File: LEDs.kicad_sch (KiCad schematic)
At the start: 14 parts

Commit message: bom, gerbers, edge cuts, footprint verification
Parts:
- D12: Vf (none) -> 1.9V
- R36, R37, R38, R39, R40, R41: P/N (none) -> CRCW0805750RFKEAHP
- R42: P/N (none) -> CRCW0805680RFKTA
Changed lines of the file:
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@@
       (effects (font (size 1.27 1.27)) hide)
     )
-    (property "Datasheet" "~" (at 224.155 97.79 0)
+    (property "Datasheet" "https://www.mouser.com/datasheet/2/216/APTD2012LCGCK-1102037.pdf" (at 224.155 97.79 0)
       (effects (font (size 1.27 1.27)) hide)
     )
@@
       (effects (font (size 1.27 1.27)) hide)
     )
+    (property "Vf" "1.9V" (at 224.155 97.79 0)
+      (effects (font (size 1.27 1.27)) hide)
+    )
     (pin "1")
     (pin "2")
@@
       (effects (font (size 1.27 1.27)) hide)
     )
+    (property "P/N" "CRCW0805680RFKTA" (at 224.155 106.68 0)
+      (effects (font (size 1.27 1.27)) hide)
+    )
     (pin "1")
     (pin "2")
@@
       (effects (font (size 1.27 1.27)) hide)
     )
-    (property "Datasheet" "~" (at 147.955 97.79 0)
+    (property "Datasheet" "https://www.mouser.com/datasheet/2/216/APT2012LSECK_J3_PRV-535674.pdf" (at 147.955 97.79 0)
       (effects (font (size 1.27 1.27)) hide)
     )
@@
       (effects (font (size 1.27 1.27)) hide)
     )
-    (property "Datasheet" "~" (at 147.955 106.68 0)
+    (property "Datasheet" "https://www.mouser.com/datasheet/2/427/dcrcwe3-1762152.pdf" (at 147.955 106.68 0)
+      (effects (font (size 1.27 1.27)) hide)
+    )
+    (property "P/N" "CRCW0805750RFKEAHP" (at 147.955 106.68 0)
       (effects (font (size 1.27 1.27)) hide)
     )
@@
       (effects (font (size 1.27 1.27)) hide)
     )
-    (property "Datasheet" "~" (at 186.055 97.79 0)
+    (property "Datasheet" "https://www.mouser.com/datasheet/2/216/APT2012LSECK_J3_PRV-535674.pdf" (at 186.055 97.79 0)
       (effects (font (size 1.27 1.27)) hide)
     )
@@
       (effects (font (size 1.27 1.27)) hide)
     )
-    (property "Datasheet" "~" (at 186.055 106.68 0)
+    (property "Datasheet" "https://www.mouser.com/datasheet/2/427/dcrcwe3-1762152.pdf" (at 186.055 106.68 0)
+      (effects (font (size 1.27 1.27)) hide)
+    )
+    (property "P/N" "CRCW0805750RFKEAHP" (at 186.055 106.68 0)
       (effects (font (size 1.27 1.27)) hide)
     )
@@
       (effects (font (size 1.27 1.27)) hide)
     )
-    (property "Datasheet" "~" (at 167.005 97.79 0)
+    (property "Datasheet" "https://www.mouser.com/datasheet/2/216/APT2012LSECK_J3_PRV-535674.pdf" (at 167.005 97.79 0)
       (effects (font (size 1.27 1.27)) hide)
     )
@@
       (effects (font (size 1.27 1.27)) hide)
     )
-    (property "Datasheet" "~" (at 167.005 106.68 0)
+    (property "Datasheet" "https://www.mouser.com/datasheet/2/427/dcrcwe3-1762152.pdf" (at 167.005 106.68 0)
+      (effects (font (size 1.27 1.27)) hide)
+    )
+    (property "P/N" "CRCW0805750RFKEAHP" (at 167.005 106.68 0)
       (effects (font (size 1.27 1.27)) hide)
     )
@@
       (effects (font (size 1.27 1.27)) hide)
     )
-    (property "Datasheet" "~" (at 205.105 97.79 0)
+    (property "Datasheet" "https://www.mouser.com/datasheet/2/216/APT2012LSECK_J3_PRV-535674.pdf" (at 205.105 97.79 0)
       (effects (font (size 1.27 1.27)) hide)
     )
@@
       (effects (font (size 1.27 1.27)) hide)
     )
-    (property "Datasheet" "~" (at 205.105 106.68 0)
+    (property "Datasheet" "https://www.mouser.com/datasheet/2/427/dcrcwe3-1762152.pdf" (at 205.105 106.68 0)
+      (effects (font (size 1.27 1.27)) hide)
+    )
+    (property "P/N" "CRCW0805750RFKEAHP" (at 205.105 106.68 0)
       (effects (font (size 1.27 1.27)) hide)
     )
@@
       (effects (font (size 1.27 1.27)) hide)
     )
-    (property "Datasheet" "~" (at 107.315 106.68 0)
+    (property "Datasheet" "https://www.mouser.com/datasheet/2/427/dcrcwe3-1762152.pdf" (at 107.315 106.68 0)
+      (effects (font (size 1.27 1.27)) hide)
+    )
+    (property "P/N" "CRCW0805750RFKEAHP" (at 107.315 106.68 0)
       (effects (font (size 1.27 1.27)) hide)
     )
@@
       (effects (font (size 1.27 1.27)) hide)
     )
-    (property "Datasheet" "~" (at 107.315 97.79 0)
+    (property "Datasheet" "https://www.mouser.com/datasheet/2/216/APT2012LSECK_J3_PRV-535674.pdf" (at 107.315 97.79 0)
       (effects (font (size 1.27 1.27)) hide)
     )
@@
       (effects (font (size 1.27 1.27)) hide)
     )
-    (property "Datasheet" "~" (at 127.635 106.68 0)
+    (property "Datasheet" "https://www.mouser.com/datasheet/2/427/dcrcwe3-1762152.pdf" (at 127.635 106.68 0)
+      (effects (font (size 1.27 1.27)) hide)
+    )
+    (property "P/N" "CRCW0805750RFKEAHP" (at 127.635 106.68 0)
       (effects (font (size 1.27 1.27)) hide)
     )
@@
       (effects (font (size 1.27 1.27)) hide)
     )
-    (property "Datasheet" "~" (at 127.635 97.79 0)
-      (effects (font (size 1.27 1.27)) hide)
-    )
+    (property "Datasheet" "https://www.mouser.com/datasheet/2/216/APT2012LSECK_J3_PRV-535674.pdf" (at 127.635 97.79 0)
+      (effects (font (size 1.27 1.27)) hide)
+    )

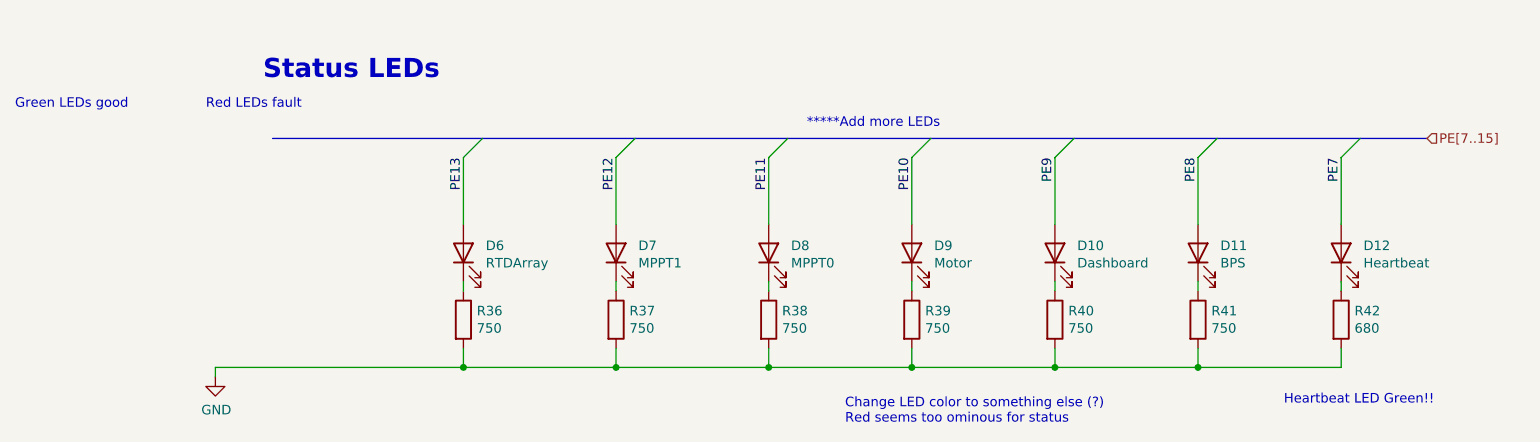
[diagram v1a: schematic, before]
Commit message: bluetooth schematic additions
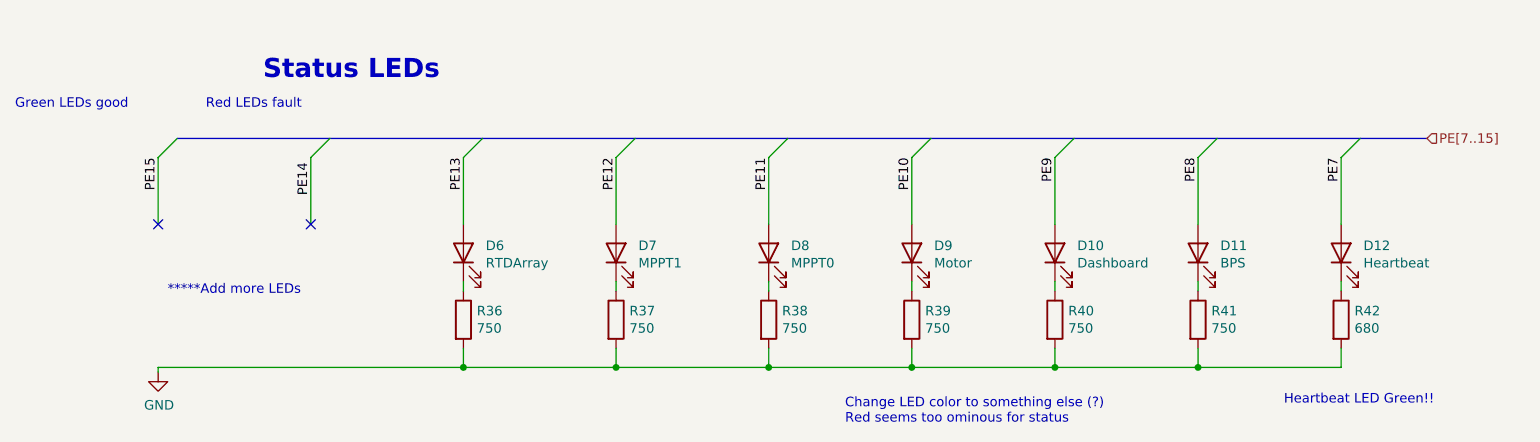
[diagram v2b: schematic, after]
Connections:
- no-connect marks 0 -> 2
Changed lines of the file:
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@@
   (junction (at 107.315 113.03) (diameter 0) (color 0 0 0 0)
   )
+  (no_connect (at 86.995 93.98))
+  (no_connect (at 66.675 93.98))
   (bus_entry (at 150.495 82.55) (size -2.54 2.54)
     (stroke (width 0) (type default))
@@
     (stroke (width 0) (type default))
   )
+  (bus_entry (at 89.535 82.55) (size -2.54 2.54)
+    (stroke (width 0) (type default))
+  )
+  (bus_entry (at 69.215 82.55) (size -2.54 2.54)
+    (stroke (width 0) (type default))
+  )
   (bus (pts (xy 207.645 82.55) (xy 226.695 82.55))
     (stroke (width 0) (type default))
   )
-  (wire (pts (xy 74.295 114.3) (xy 74.295 113.03))
+  (wire (pts (xy 66.675 113.665) (xy 66.675 113.03))
     (stroke (width 0) (type default))
   )
@@
     (stroke (width 0) (type default))
   )
+  (wire (pts (xy 66.675 93.98) (xy 66.675 85.09))
+    (stroke (width 0) (type default))
+  )
   (wire (pts (xy 127.635 113.03) (xy 127.635 110.49))
     (stroke (width 0) (type default))
@@
     (stroke (width 0) (type default))
   )
-  (wire (pts (xy 107.315 93.98) (xy 107.315 85.09))
-    (stroke (width 0) (type default))
-  )
   (wire (pts (xy 167.005 93.98) (xy 167.005 85.09))
     (stroke (width 0) (type default))
@@
     (stroke (width 0) (type default))
   )
+  (bus (pts (xy 89.535 82.55) (xy 109.855 82.55))
+    (stroke (width 0) (type default))
+  )
+  (wire (pts (xy 86.995 85.09) (xy 86.995 93.98))
+    (stroke (width 0) (type default))
+  )
   (wire (pts (xy 224.155 93.98) (xy 224.155 85.09))
     (stroke (width 0) (type default))
@@
     (stroke (width 0) (type default))
   )
-  (wire (pts (xy 74.295 113.03) (xy 107.315 113.03))
-    (stroke (width 0) (type default))
-  )
-  (bus (pts (xy 81.915 82.55) (xy 109.855 82.55))
+  (wire (pts (xy 66.675 113.03) (xy 107.315 113.03))
+    (stroke (width 0) (type default))
+  )
+  (bus (pts (xy 69.215 82.55) (xy 89.535 82.55))
     (stroke (width 0) (type default))
   )
@@
   )
   (wire (pts (xy 107.315 113.03) (xy 107.315 110.49))
+    (stroke (width 0) (type default))
+  )
+  (wire (pts (xy 107.315 85.09) (xy 107.315 93.98))
     (stroke (width 0) (type default))
   )
@@
     (effects (font (size 1.27 1.27)) (justify left bottom))
   )
-  (text "*****Add more LEDs" (at 153.035 81.28 0)
+  (text "*****Add more LEDs" (at 67.945 103.505 0)
     (effects (font (size 1.27 1.27)) (justify left bottom))
   )
@@
     (effects (font (size 1.27 1.27)) (justify left bottom))
   )
+  (label "PE14" (at 86.995 85.725 270) (fields_autoplaced)
+    (effects (font (size 1.27 1.27)) (justify right bottom))
+  )
   (label "PE9" (at 186.055 85.09 270) (fields_autoplaced)
+    (effects (font (size 1.27 1.27)) (justify right bottom))
+  )
+  (label "PE15" (at 66.675 85.09 270) (fields_autoplaced)
     (effects (font (size 1.27 1.27)) (justify right bottom))
   )
@@
       (effects (font (size 1.27 1.27)) hide)
     )
-    (property "Datasheet" "~" (at 224.155 106.68 0)
+    (property "Datasheet" "https://www.mouser.com/datasheet/2/427/dcrcwe3-1762152.pdf" (at 224.155 106.68 0)
       (effects (font (size 1.27 1.27)) hide)
     )
@@
     )
   )
-  (symbol (lib_id "power:GND") (at 74.295 114.3 0) (unit 1)
-    (in_bom yes) (on_board yes) (dnp no)
-    (property "Reference" "#PWR0176" (at 74.295 120.65 0)
-      (effects (font (size 1.27 1.27)) hide)
-    )
-    (property "Value" "GND" (at 74.422 118.6942 0)
+  (symbol (lib_id "power:GND") (at 66.675 113.665 0) (unit 1)
+    (in_bom yes) (on_board yes) (dnp no)
+    (property "Reference" "#PWR0176" (at 66.675 120.015 0)
+      (effects (font (size 1.27 1.27)) hide)
+    )
+    (property "Value" "GND" (at 66.802 118.0592 0)
       (effects (font (size 1.27 1.27)))
     )
-    (property "Footprint" "" (at 74.295 114.3 0)
-      (effects (font (size 1.27 1.27)) hide)
-    )
-    (property "Datasheet" "" (at 74.295 114.3 0)
-      (effects (font (size 1.27 1.27)) hide)
-    )
+    (property "Footprint" "" (at 66.675 113.665 0)
+      (effects (font (size 1.27 1.27)) hide)
+    )
+    (property "Datasheet" "" (at 66.675 113.665 0)
+      (effects (font (size 1.27 1.27)) hide)
+    )

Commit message: began input/breakout changes
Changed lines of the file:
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@@
     (effects (font (size 1.27 1.27)) (justify left bottom))
   )
-  (text "Red LEDs fault" (at 73.025 78.74 0)
+  (text "Red LEDs fault" (at 69.215 76.835 0)
     (effects (font (size 1.27 1.27)) (justify left bottom))
   )
-  (text "Status LEDs" (at 80.645 74.93 0)
+  (text "Status LEDs" (at 68.58 70.485 0)
     (effects (font (size 2.54 2.54) (thickness 0.508) bold) (justify left bottom))
   )
-  (text "Green LEDs good" (at 47.625 78.74 0)
+  (text "Green LEDs good" (at 69.215 73.66 0)
     (effects (font (size 1.27 1.27)) (justify left bottom))
   )

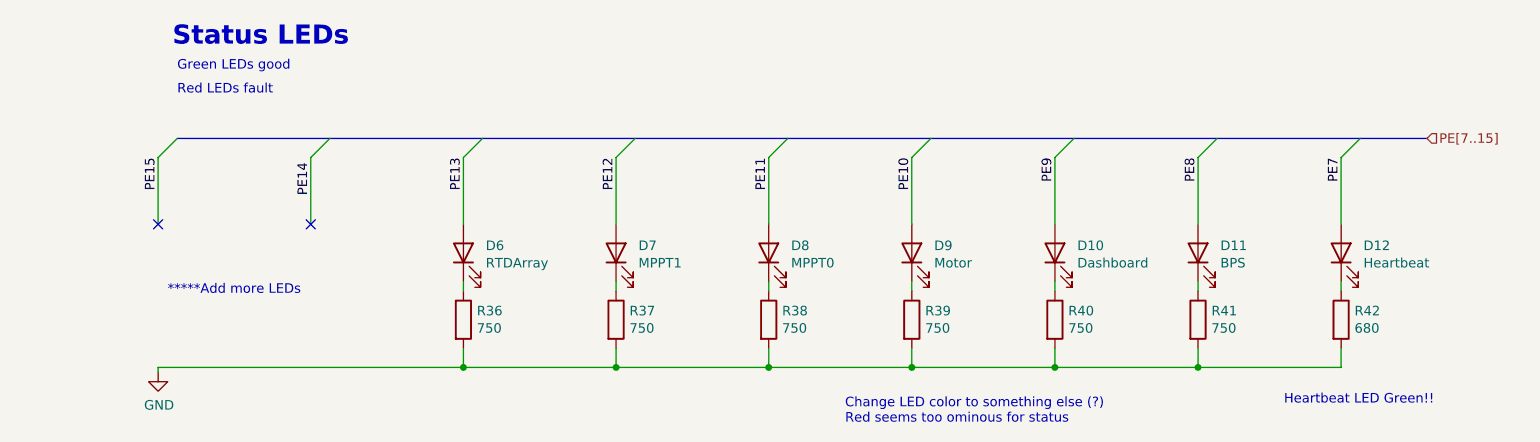
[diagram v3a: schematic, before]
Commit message: led fix + notes
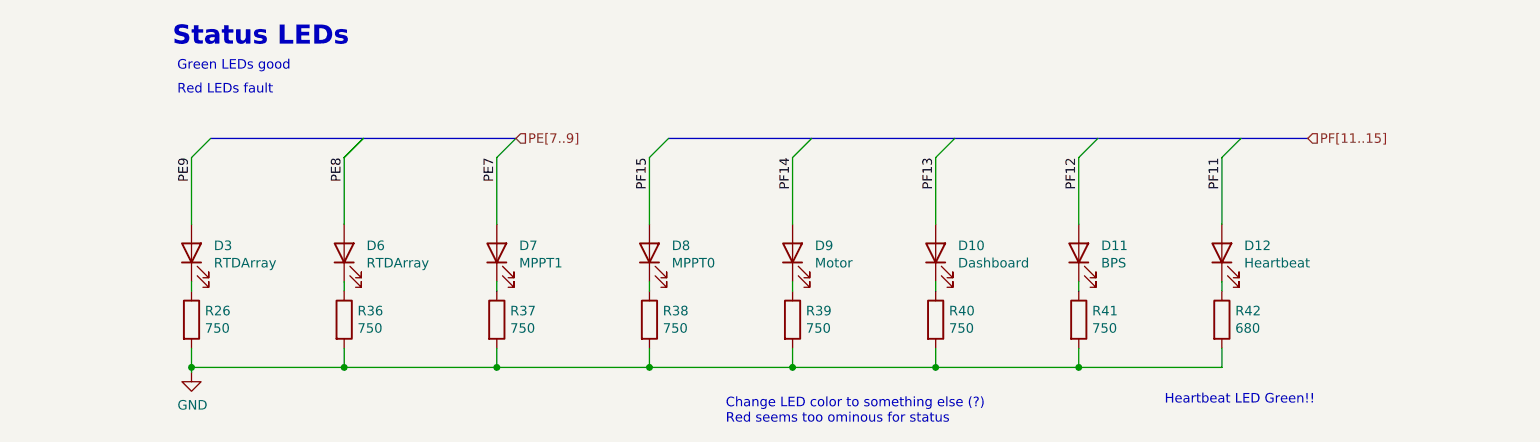
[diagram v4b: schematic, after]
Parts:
- added D3: RTDArray, LED_SMD:LED_0805_2012Metric, symbol Device:LED
- added R26: 750, Resistor_SMD:R_0805_2012Metric, symbol Device:R
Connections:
- net PE12 is gone; now on net PE7: D7.2 (A)
- net PE13 is gone; now on net PE8: D6.2 (A)
- net GND: now also R26.2
- net PE7: no longer D12.2 (A)
- net PE8: no longer D11.2 (A)
- net PE9: now also D3.2 (A); no longer D10.2 (A)
- net PE10 renamed PF14
- net PE11 renamed PF15
- new net: D3.1 (K), R26.1
- new net PF11: D12.2 (A)
- new net PF12: D11.2 (A)
- new net PF13: D10.2 (A)
- no-connect marks 2 -> 0
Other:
- note removed: "*****Add more LEDs"
- moved on the sheet: D10, D11, D12, D6, D7, D8, D9, R36, R37, R38, R39, R40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

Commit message: inputs routing + fixed models + clock keepouts
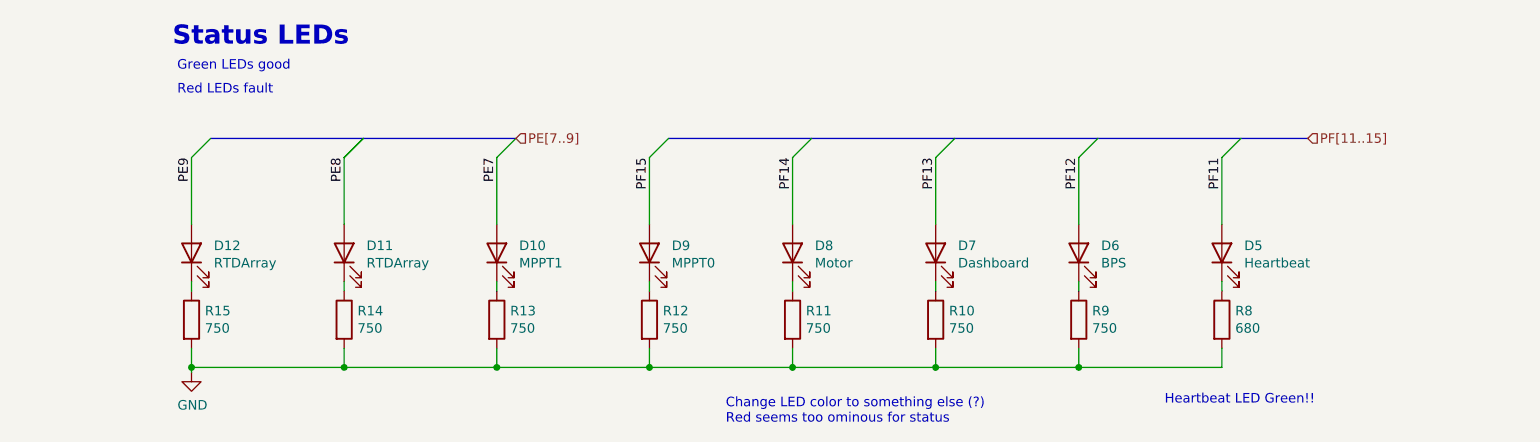
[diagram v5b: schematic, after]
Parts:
- renumbered D7 to D10, D6 to D11, D3 to D12, D12 to D5, D11 to D6, D10 to D7, D9 to D8, D8 to D9, R40 to R10, R39 to R11, R38 to R12, R37 to R13, R36 to R14, R26 to R15, R42 to R8, R41 to R9
